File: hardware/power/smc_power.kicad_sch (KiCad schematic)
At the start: 66 parts, among them IC1 LM393DR2GH, J1 Screw_Terminal_Input, J2 Screw_Terminal_Output, Q1 P40B10SL, U1 TPS54360DDA, U2 AP2112K-3.3, U3 TPS54360DDA, U5 MCP1416, U6 TL431B_C54830630, U7 L78L12_SOT89

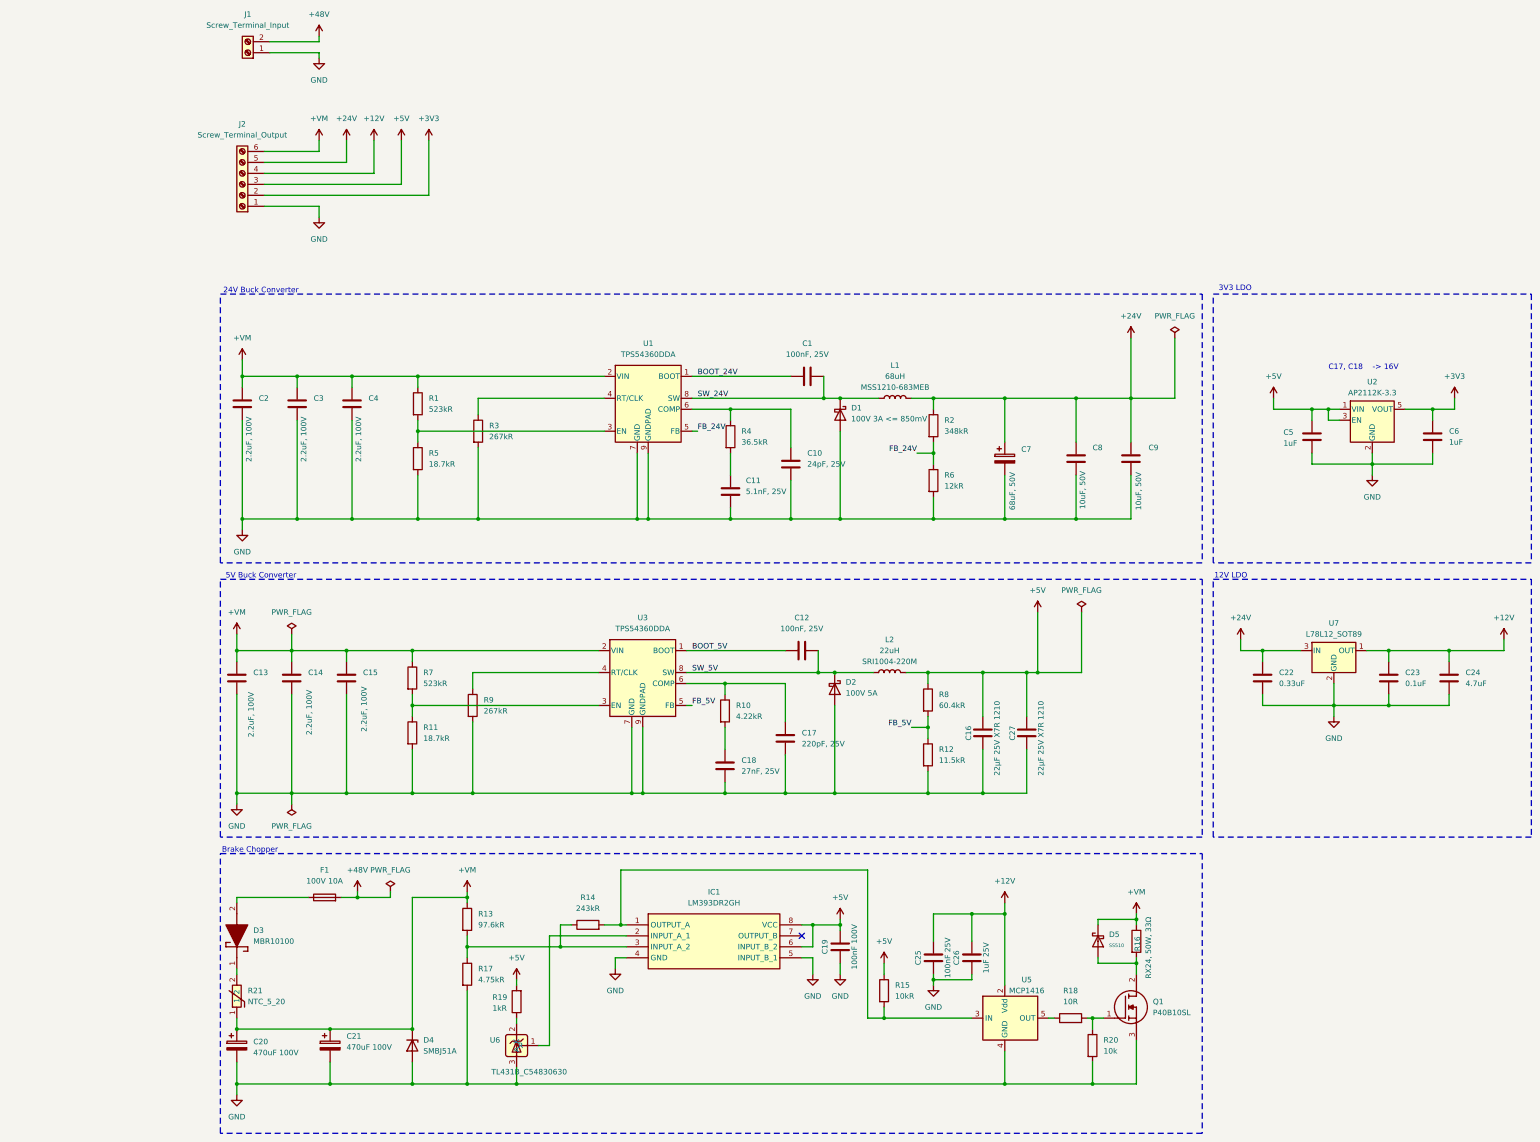
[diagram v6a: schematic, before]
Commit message: hw(power): minor review items (NTC 5D-20 + footprint, notes), AP2112K load note, refs #35
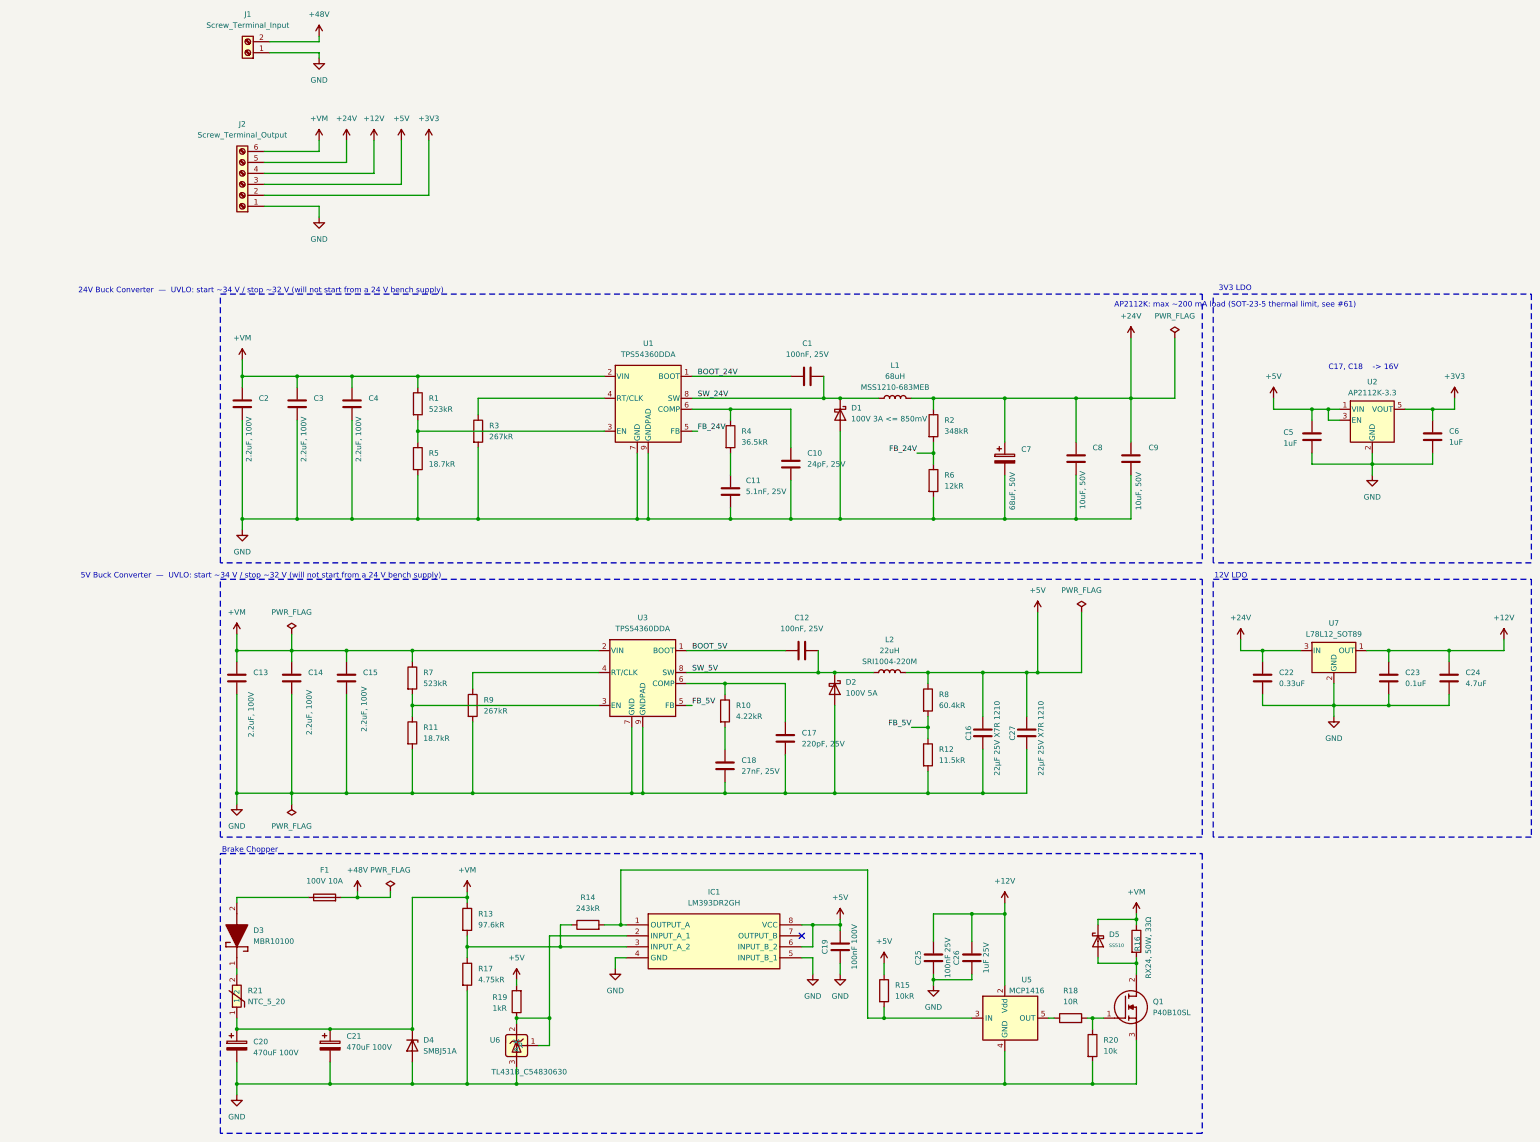
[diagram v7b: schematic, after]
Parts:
- C16, C27: footprint (none) -> Capacitor_SMD:C_1210_3225Metric_Pad1.33x2.70mm_HandSolder
- C22, C23, C24: footprint Package_TO_SOT_SMD:SOT-89-3 -> Capacitor_SMD:C_0805_2012Metric_Pad1.18x1.45mm_HandSolder
- R21: footprint Connector_Phoenix_SPT:PhoenixContact_SPT_5_1-V-7.5_1x01_P7.5mm_Vertical -> Step Motor Controller:NTC_Disc_D13mm_W5.5mm_P7.5mm
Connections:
- net at R19.1, U6.2 (K): now also IC1.2 (INPUT_A_1), U6.1 (R)
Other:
- note added: "24V Buck Converter — UVLO: start ~34 V / stop ~32 V (will not start from a 24 V bench supply)"
- note added: "5V Buck Converter — UVLO: start ~34 V / stop ~32 V (will not start from a 24 V bench supply)"
- note added: "AP2112K: max ~200 mA load (SOT-23-5 thermal limit, see #61)"
- note removed: "24V Buck Converter"
- note removed: "5V Buck Converter"
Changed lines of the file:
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@@
 		)
 	)
-	(text "5V Buck Converter"
+	(text "5V Buck Converter  —  UVLO: start ~34 V / stop ~32 V (will not start from a 24 V bench supply)"
 		(exclude_from_sim no)
 		(at 27.178 150.368 0)
@@
 		)
 	)
+(text "AP2112K: max ~200 mA load (SOT-23-5 thermal limit, see #61)"
+		(exclude_from_sim no)
+		(at 252.73 87.63 0)
+		(effects
+			(font
+				(size 1.27 1.27)
+			)
+		)
+	)
 	(text "C17, C18	-> 16V"
 		(exclude_from_sim no)
@@
 		)
 	)
-	(text "24V Buck Converter"
+	(text "24V Buck Converter  —  UVLO: start ~34 V / stop ~32 V (will not start from a 24 V bench supply)"
 		(exclude_from_sim no)
 		(at 27.178 84.328 0)
@@
 	(wire
 		(pts
+			(xy 86.36 252.73) (xy 93.98 252.73)
+		)
+		(stroke
+			(width 0)
+			(type default)
+		)
+	)
+	(junction
+		(at 86.36 252.73)
+		(diameter 0)
+		(color 0 0 0 0)
+	)
+	(junction
+		(at 93.98 252.73)
+		(diameter 0)
+		(color 0 0 0 0)
+	)
+	(wire
+		(pts
 			(xy 207.01 158.75) (xy 207.01 172.72)
 		)
@@
 			)
 		)
-		(property "Footprint" ""
+		(property "Footprint" "Capacitor_SMD:C_1210_3225Metric_Pad1.33x2.70mm_HandSolder"
 			(at 205.4352 190.5 0)
 			(hide yes)
@@
 			)
 		)
-		(property "Footprint" "Package_TO_SOT_SMD:SOT-89-3"
+		(property "Footprint" "Capacitor_SMD:C_0805_2012Metric_Pad1.18x1.45mm_HandSolder"
 			(at 260.0452 177.8 0)
 			(hide yes)
@@
 			)
 		)
-		(property "Footprint" "Package_TO_SOT_SMD:SOT-89-3"
+		(property "Footprint" "Capacitor_SMD:C_0805_2012Metric_Pad1.18x1.45mm_HandSolder"
 			(at 303.2252 177.8 0)
 			(hide yes)
@@
 			)
 		)
-		(property "Footprint" "Connector_Phoenix_SPT:PhoenixContact_SPT_5_1-V-7.5_1x01_P7.5mm_Vertical"
+		(property "Footprint" "Step Motor Controller:NTC_Disc_D13mm_W5.5mm_P7.5mm"
 			(at 21.59 247.65 0)
 			(hide yes)
@@
 			)
 		)
-		(property "Footprint" "Package_TO_SOT_SMD:SOT-89-3"
+		(property "Footprint" "Capacitor_SMD:C_0805_2012Metric_Pad1.18x1.45mm_HandSolder"
 			(at 289.2552 177.8 0)
 			(hide yes)
@@
 			)
 		)
-		(property "Footprint" ""
+		(property "Footprint" "Capacitor_SMD:C_1210_3225Metric_Pad1.33x2.70mm_HandSolder"
 			(at 195.2752 190.5 0)
 			(hide yes)

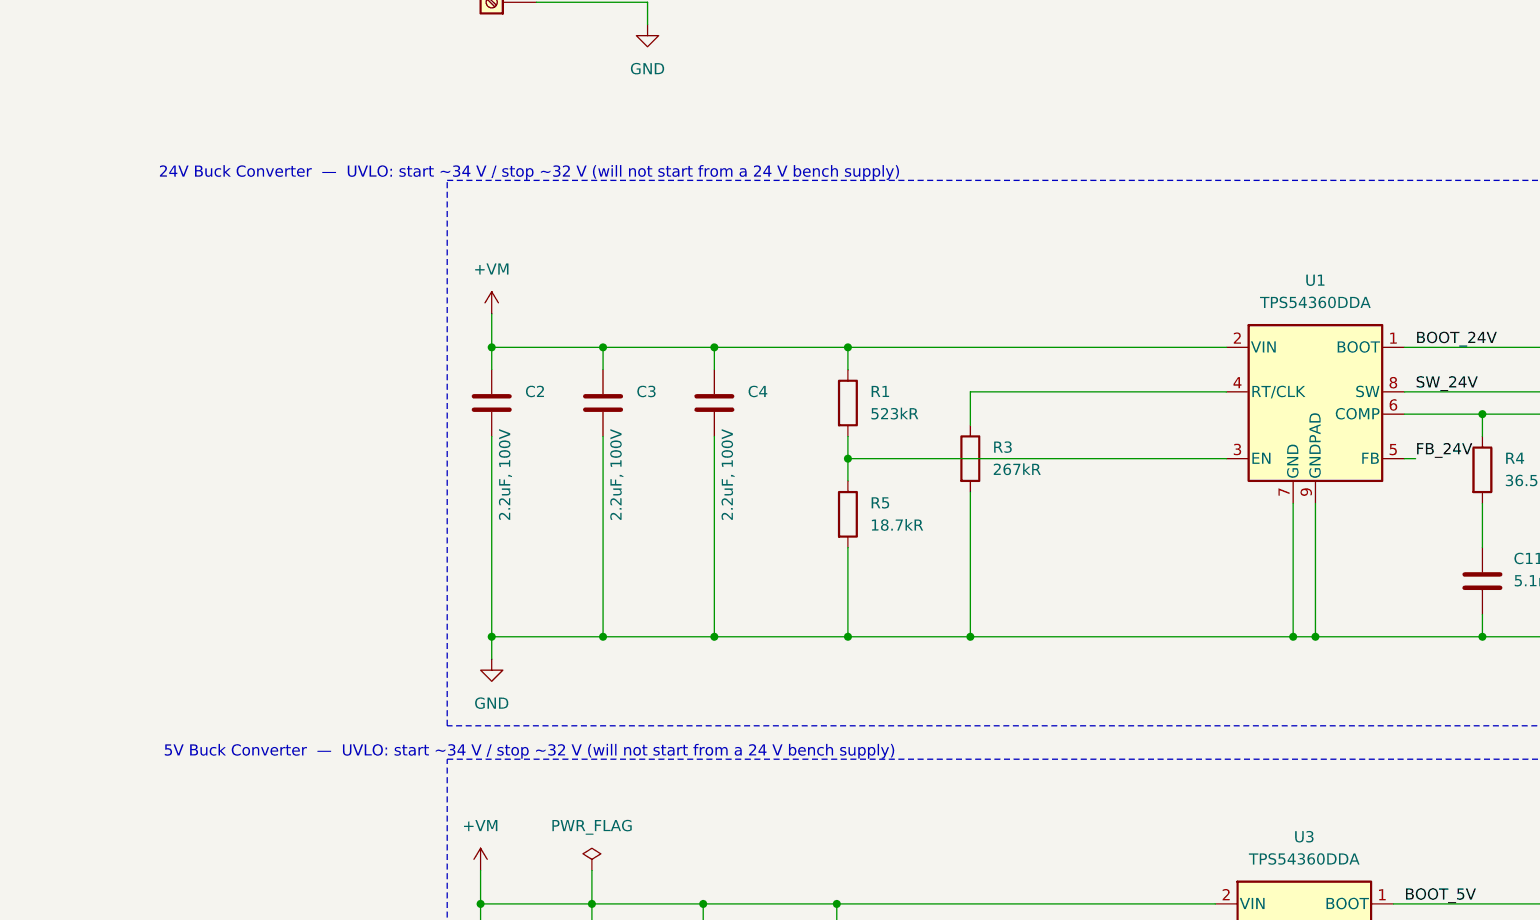
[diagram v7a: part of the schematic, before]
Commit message: hw(power): NTC R21 LCSC -> C122780 (5D-20), refs #48
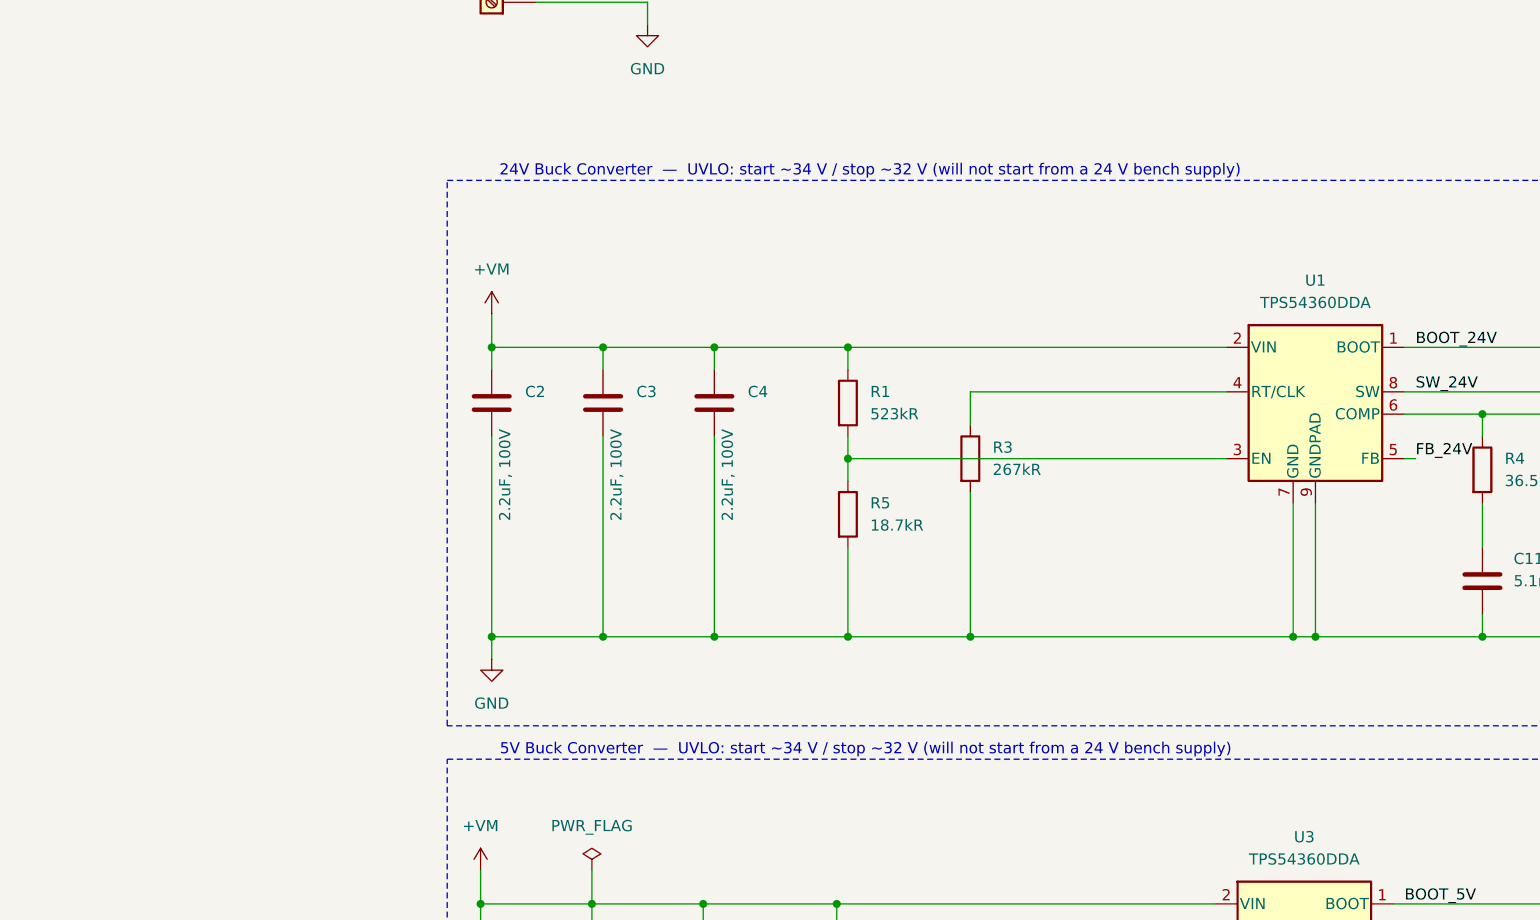
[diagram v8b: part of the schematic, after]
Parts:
- R21: LCSC C72676 -> C122780
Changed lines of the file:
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@@
 	(text "5V Buck Converter  —  UVLO: start ~34 V / stop ~32 V (will not start from a 24 V bench supply)"
 		(exclude_from_sim no)
-		(at 27.178 150.368 0)
+		(at 65.532 150.114 0)
 		(effects
 			(font
@@
 		)
 	)
-(text "AP2112K: max ~200 mA load (SOT-23-5 thermal limit, see #61)"
+	(text "C17, C18	-> 16V"
 		(exclude_from_sim no)
-		(at 252.73 87.63 0)
+		(at 282.448 102.108 0)
 		(effects
 			(font
@@
 		)
 	)
-	(text "C17, C18	-> 16V"
+	(text "AP2112K: max ~200 mA load (SOT-23-5 thermal limit, see #61)"
 		(exclude_from_sim no)
-		(at 282.448 102.108 0)
+		(at 252.73 87.63 0)
 		(effects
 			(font
@@
 	(text "24V Buck Converter  —  UVLO: start ~34 V / stop ~32 V (will not start from a 24 V bench supply)"
 		(exclude_from_sim no)
-		(at 27.178 84.328 0)
+		(at 66.04 84.074 0)
 		(effects
 			(font
@@
 	)
 	(junction
+		(at 86.36 252.73)
+		(diameter 0)
+		(color 0 0 0 0)
+	)
+	(junction
 		(at 114.3 137.16)
 		(diameter 0)
@@
 	)
 	(junction
+		(at 93.98 252.73)
+		(diameter 0)
+		(color 0 0 0 0)
+	)
+	(junction
 		(at 161.29 231.14)
 		(diameter 0)
@@
 	(wire
 		(pts
-			(xy 86.36 252.73) (xy 93.98 252.73)
-		)
-		(stroke
-			(width 0)
-			(type default)
-		)
-	)
-	(junction
-		(at 86.36 252.73)
-		(diameter 0)
-		(color 0 0 0 0)
-	)
-	(junction
-		(at 93.98 252.73)
-		(diameter 0)
-		(color 0 0 0 0)
-	)
-	(wire
-		(pts
 			(xy 207.01 158.75) (xy 207.01 172.72)
 		)
@@
 	(wire
 		(pts
+			(xy 86.36 252.73) (xy 93.98 252.73)
+		)
+		(stroke
+			(width 0)
+			(type default)
+		)
+	)
+	(wire
+		(pts
 			(xy 161.29 231.14) (xy 161.29 229.87)
 		)
@@
 			)
 		)
-		(property "LCSC" "C72676"
+		(property "LCSC" "C122780"
 			(at 21.59 247.65 0)
 			(hide yes)
